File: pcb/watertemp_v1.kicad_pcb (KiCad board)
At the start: 2 copper layers, 56 x 90 mm, 54 parts, among them J1 RN2483 Ext, J2 SWD, J3 I2C, J4 UART1, J5 UART2, Q1 Q_PMOS_GSD, U1 LPC11U24FBD48, U2 RN2483, U3 SHT21, U4 LP5907-Q1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

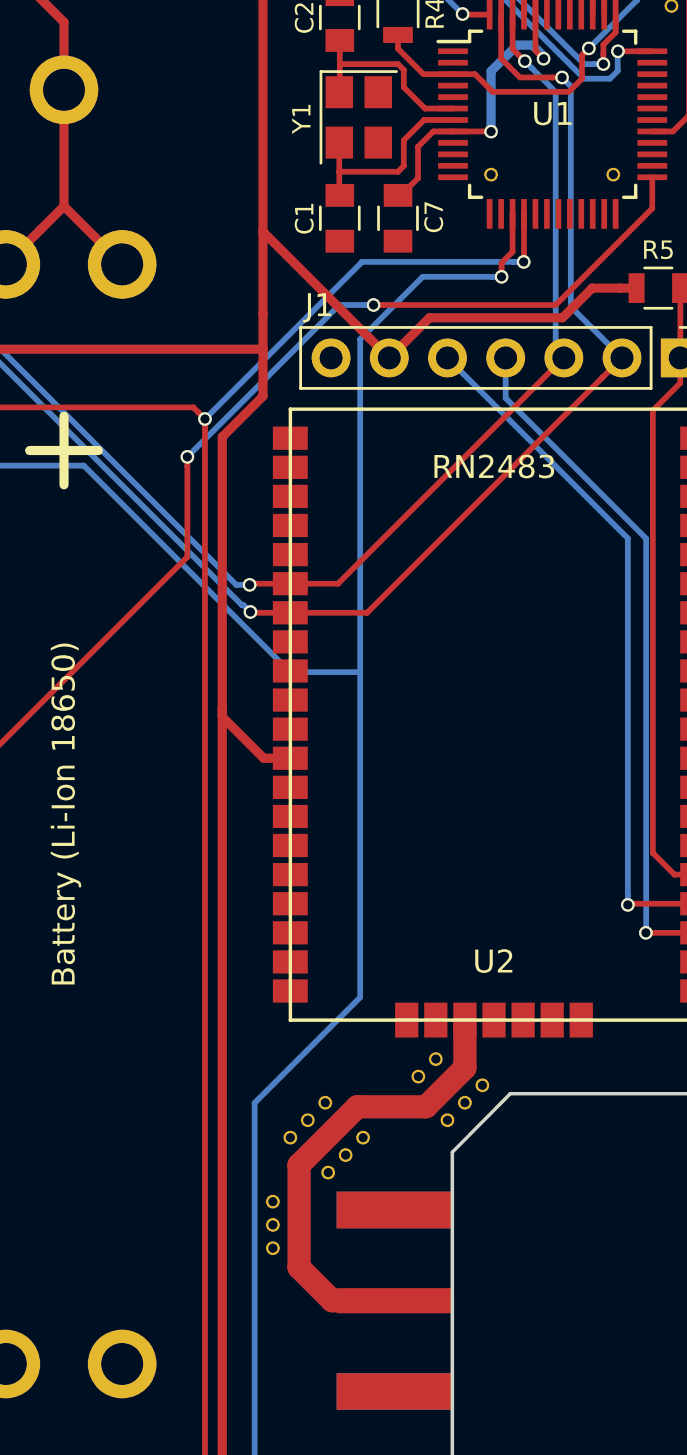
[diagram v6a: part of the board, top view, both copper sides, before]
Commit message: Fix oscillator symbol/footprint (fixes #10)
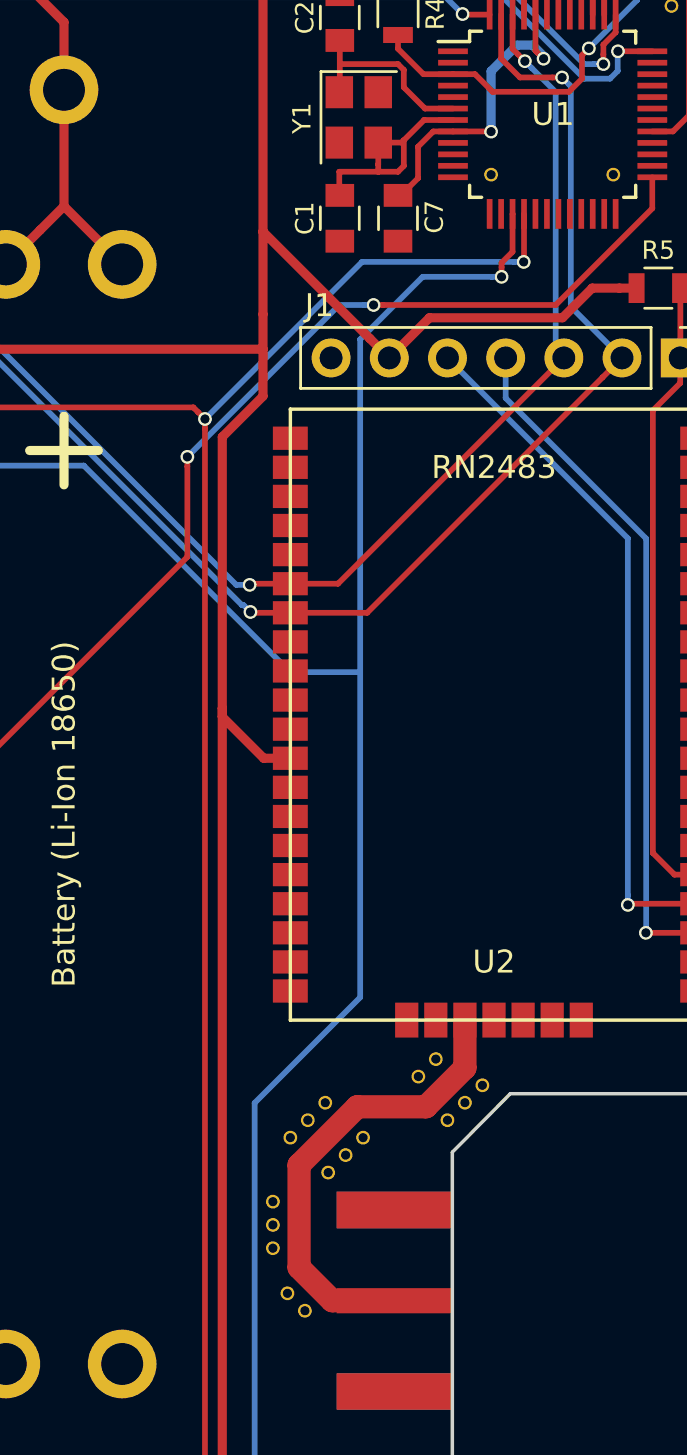
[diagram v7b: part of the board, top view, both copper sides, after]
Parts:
- added REF**: VIA-0.6mm, StitchingVia:VIA-0.6mm, F.Cu at (59.6, 113.5)
- added REF**: VIA-0.6mm, StitchingVia:VIA-0.6mm, F.Cu at (58.8, 112.7)
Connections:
- Y1 pad 2: Net-(C1-Pad1) -> GND
- Y1 pad 3: (no net) -> Net-(C1-Pad1)
- Y1 pad 4: (no net) -> GND
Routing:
- net Net-(C1-Pad1): track 8.87 -> 10.0 mm
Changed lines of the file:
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@@
 (kicad_pcb (version 4) (host pcbnew 4.0.6)
   (general
-    (links 113)
+    (links 120)
     (no_connects 0)
     (area 26.924999 39.924999 83.075001 130.075001)
     (thickness 1.6)
     (drawings 28)
-    (tracks 324)
+    (tracks 329)
     (zones 0)
-    (modules 54)
+    (modules 56)
     (nets 81)
   )
@@
   )
   (module StitchingVia:VIA-0.6mm (layer F.Cu)
+    (at 59.563 113.4745 90)
+    (fp_text reference REF** (at 0 1.27 90) (layer F.SilkS) hide
+      (effects (font (size 1 1) (thickness 0.15)))
+    )
+    (fp_text value VIA-0.6mm (at 0 -1.27 90) (layer F.Fab) hide
+      (effects (font (size 1 1) (thickness 0.15)))
+    )
+    (pad 1 thru_hole circle (at 0 0 90) (size 0.6 0.6) (drill 0.4) (layers *.Cu)
+      (net 1 GND) (zone_connect 2))
+  )
+  (module StitchingVia:VIA-0.6mm (layer F.Cu)
+    (at 58.801 112.7125 90)
+    (fp_text reference REF** (at 0 1.27 90) (layer F.SilkS) hide
+      (effects (font (size 1 1) (thickness 0.15)))
+    )
+    (fp_text value VIA-0.6mm (at 0 -1.27 90) (layer F.Fab) hide
+      (effects (font (size 1 1) (thickness 0.15)))
+    )
+    (pad 1 thru_hole circle (at 0 0 90) (size 0.6 0.6) (drill 0.4) (layers *.Cu)
+      (net 1 GND) (zone_connect 2))
+  )
+  (module StitchingVia:VIA-0.6mm (layer F.Cu)
     (at 58.166 110.744)
     (fp_text reference REF** (at 0 1.27) (layer F.SilkS) hide
@@
       (net 5 "Net-(C2-Pad1)"))
     (pad 2 smd rect (at 1.1 0.85 270) (size 1.4 1.2) (layers F.Cu F.Paste F.Mask)
+      (net 1 GND))
+    (pad 3 smd rect (at 1.1 -0.85 270) (size 1.4 1.2) (layers F.Cu F.Paste F.Mask)
       (net 4 "Net-(C1-Pad1)"))
-    (pad 3 smd rect (at 1.1 -0.85 270) (size 1.4 1.2) (layers F.Cu F.Paste F.Mask))
-    (pad 4 smd rect (at -1.1 -0.85 270) (size 1.4 1.2) (layers F.Cu F.Paste F.Mask))
+    (pad 4 smd rect (at -1.1 -0.85 270) (size 1.4 1.2) (layers F.Cu F.Paste F.Mask)
+      (net 1 GND))
     (model ${KISYS3DMOD}/Crystals.3dshapes/Crystal_SMD_SeikoEpson_TSX3225-4pin_3.2x2.5mm.wrl
       (at (xyz 0 0 0))
@@
   (segment (start 49.0474 60.1786) (end 49.0474 65.2586) (width 0.4) (layer F.Cu) (net 3))
   (segment (start 49.0474 65.2586) (end 51.5874 67.7986) (width 0.4) (layer F.Cu) (net 3))
-  (segment (start 61.065 63.754) (end 63.627 63.754) (width 0.25) (layer F.Cu) (net 4))
+  (segment (start 61.065 63.754) (end 62.7634 63.754) (width 0.25) (layer F.Cu) (net 4))
+  (segment (start 62.7634 63.754) (end 63.627 63.754) (width 0.25) (layer F.Cu) (net 4))
+  (segment (start 62.765 62.482) (end 62.765 63.432) (width 0.25) (layer F.Cu) (net 4))
+  (segment (start 62.765 63.432) (end 62.7634 63.4336) (width 0.25) (layer F.Cu) (net 4))
+  (segment (start 62.7634 63.4336) (end 62.7634 63.754) (width 0.25) (layer F.Cu) (net 4))
+  (segment (start 63.881 63.5) (end 63.881 62.3824) (width 0.25) (layer F.Cu) (net 4))
   (segment (start 63.627 63.754) (end 63.881 63.5) (width 0.25) (layer F.Cu) (net 4))
-  (segment (start 63.881 63.5) (end 63.881 62.3824) (width 0.25) (layer F.Cu) (net 4))
+  (segment (start 61.065 63.754) (end 61.065 64.764) (width 0.25) (layer F.Cu) (net 4))
+  (segment (start 61.065 64.764) (end 61.087 64.786) (width 0.25) (layer F.Cu) (net 4))
+  (segment (start 63.881 62.3824) (end 63.7814 62.482) (width 0.25) (layer F.Cu) (net 4))
+  (segment (start 63.7814 62.482) (end 62.765 62.482) (width 0.25) (layer F.Cu) (net 4))
   (segment (start 63.881 62.3824) (end 64.77 61.4934) (width 0.25) (layer F.Cu) (net 4))
   (segment (start 64.77 61.4934) (end 64.7726 61.496) (width 0.25) (layer F.Cu) (net 4))
   (segment (start 64.7726 61.496) (end 66.028 61.496) (width 0.25) (layer F.Cu) (net 4))
-  (segment (start 61.065 63.754) (end 61.065 64.764) (width 0.25) (layer F.Cu) (net 4))
-  (segment (start 61.065 62.482) (end 61.065 63.754) (width 0.25) (layer F.Cu) (net 4))
-  (segment (start 61.065 64.764) (end 61.087 64.786) (width 0.25) (layer F.Cu) (net 4))
   (segment (start 61.087 59.055) (end 63.627 59.055) (width 0.25) (layer F.Cu) (net 5))
   (segment (start 63.627 59.055) (end 63.881 59.309) (width 0.25) (layer F.Cu) (net 5))

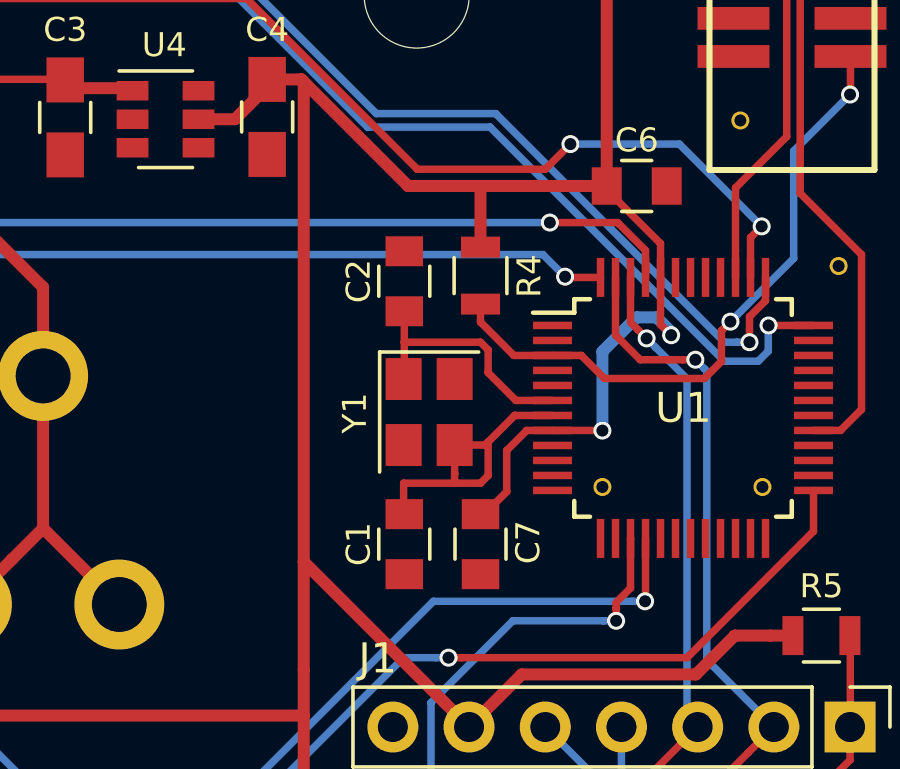
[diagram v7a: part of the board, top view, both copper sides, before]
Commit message: Move oscillator closer µC
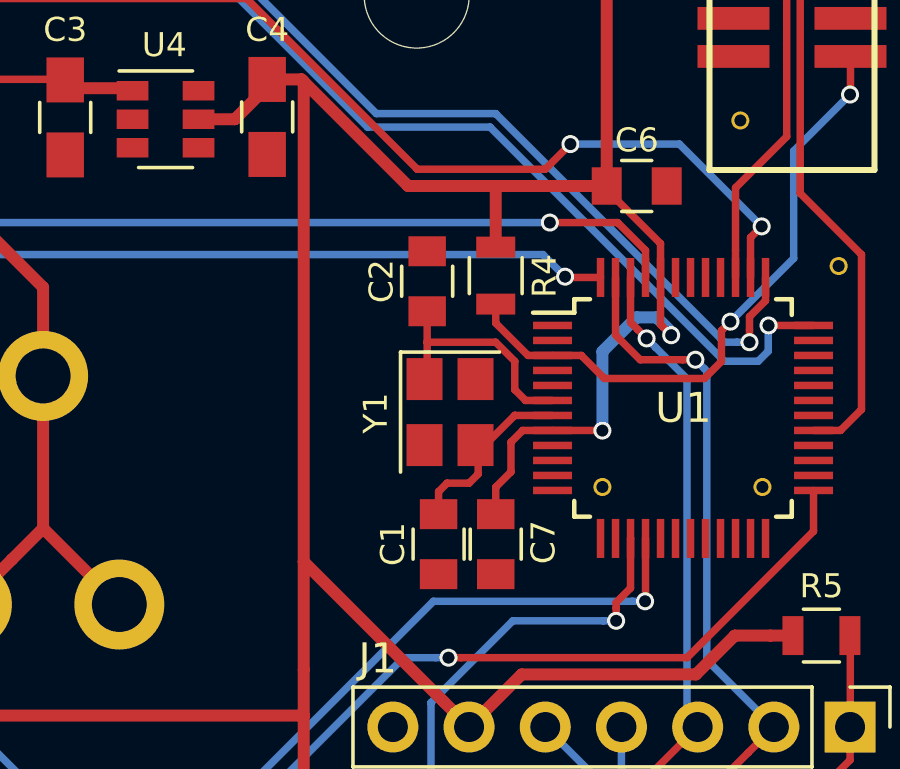
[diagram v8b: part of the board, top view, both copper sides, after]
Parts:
- moved C1 1.14 mm to (62.2, 65.8)
- moved C2 0.76 mm to (61.8, 57.0)
- moved Y1 0.70 mm to (62.6, 61.4)
- moved C7 0.51 mm to (64.1, 65.8)
- moved R4 0.51 mm to (64.1, 56.8)
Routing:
- net Net-(C1-Pad1): track 10.0 -> 5.94 mm
- net Net-(C2-Pad1): track 8.46 -> 7.80 mm
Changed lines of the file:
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@@
-(kicad_pcb (version 4) (host pcbnew 4.0.6)
+(kicad_pcb (version 4) (host pcbnew 4.0.7)
   (general
     (links 120)
-    (no_connects 0)
-    (area 26.924999 39.924999 83.075001 130.075001)
+    (no_connects 4)
+    (area 22.966905 37.719 91.100001 131.826001)
     (thickness 1.6)
     (drawings 28)
-    (tracks 329)
+    (tracks 323)
     (zones 0)
     (modules 56)
@@
   )
   (module Capacitors_SMD:C_0805 (layer F.Cu)
-    (at 61.087 65.786 270)
+    (at 62.23 65.786 270)
     (descr "Capacitor SMD 0805, reflow soldering, AVX (see smccp.pdf)")
     (tags "capacitor 0805")
@@
   )
   (module Capacitors_SMD:C_0805 (layer F.Cu)
-    (at 61.087 57.023 90)
+    (at 61.849 57.023 90)
     (descr "Capacitor SMD 0805, reflow soldering, AVX (see smccp.pdf)")
     (tags "capacitor 0805")
@@
   )
   (module Crystals:Crystal_SMD_Abracon_ABM8G-4pin_3.2x2.5mm (layer F.Cu)
-    (at 61.915 61.382 270)
+    (at 62.611 61.384 270)
     (descr "Abracon Miniature Ceramic Smd Crystal ABM8G http://www.abracon.com/Resonators/ABM8G.pdf, 3.2x2.5mm^2 package")
     (tags "SMD SMT crystal")
@@
   )
   (module Capacitors_SMD:C_0805 (layer F.Cu)
-    (at 63.627 65.786 90)
+    (at 64.135 65.786 90)
     (descr "Capacitor SMD 0805, reflow soldering, AVX (see smccp.pdf)")
     (tags "capacitor 0805")
@@
   )
   (module Resistors_SMD:R_0805 (layer F.Cu)
-    (at 63.627 56.835 270)
+    (at 64.135 56.835 270)
     (descr "Resistor SMD 0805, reflow soldering, Vishay (see dcrcw.pdf)")
     (tags "resistor 0805")
@@
   (segment (start 49.0474 60.1786) (end 49.0474 65.2586) (width 0.4) (layer F.Cu) (net 3))
   (segment (start 49.0474 65.2586) (end 51.5874 67.7986) (width 0.4) (layer F.Cu) (net 3))
-  (segment (start 61.065 63.754) (end 62.7634 63.754) (width 0.25) (layer F.Cu) (net 4))
-  (segment (start 62.7634 63.754) (end 63.627 63.754) (width 0.25) (layer F.Cu) (net 4))
-  (segment (start 62.765 62.482) (end 62.765 63.432) (width 0.25) (layer F.Cu) (net 4))
-  (segment (start 62.765 63.432) (end 62.7634 63.4336) (width 0.25) (layer F.Cu) (net 4))
-  (segment (start 62.7634 63.4336) (end 62.7634 63.754) (width 0.25) (layer F.Cu) (net 4))
-  (segment (start 63.881 63.5) (end 63.881 62.3824) (width 0.25) (layer F.Cu) (net 4))
-  (segment (start 63.627 63.754) (end 63.881 63.5) (width 0.25) (layer F.Cu) (net 4))
-  (segment (start 61.065 63.754) (end 61.065 64.764) (width 0.25) (layer F.Cu) (net 4))
-  (segment (start 61.065 64.764) (end 61.087 64.786) (width 0.25) (layer F.Cu) (net 4))
+  (segment (start 63.246 63.754) (end 63.549 63.451) (width 0.25) (layer F.Cu) (net 4))
+  (segment (start 63.549 63.451) (end 63.549 62.484) (width 0.25) (layer F.Cu) (net 4))
+  (segment (start 62.512 63.754) (end 63.246 63.754) (width 0.25) (layer F.Cu) (net 4))
+  (segment (start 62.23 64.786) (end 62.23 64.036) (width 0.25) (layer F.Cu) (net 4))
+  (segment (start 62.23 64.036) (end 62.512 63.754) (width 0.25) (layer F.Cu) (net 4))
   (segment (start 63.881 62.3824) (end 63.7814 62.482) (width 0.25) (layer F.Cu) (net 4))
-  (segment (start 63.7814 62.482) (end 62.765 62.482) (width 0.25) (layer F.Cu) (net 4))
   (segment (start 63.881 62.3824) (end 64.77 61.4934) (width 0.25) (layer F.Cu) (net 4))
   (segment (start 64.77 61.4934) (end 64.7726 61.496) (width 0.25) (layer F.Cu) (net 4))
   (segment (start 64.7726 61.496) (end 66.028 61.496) (width 0.25) (layer F.Cu) (net 4))
-  (segment (start 61.087 59.055) (end 63.627 59.055) (width 0.25) (layer F.Cu) (net 5))
-  (segment (start 63.627 59.055) (end 63.881 59.309) (width 0.25) (layer F.Cu) (net 5))
-  (segment (start 63.881 59.309) (end 63.881 60.071) (width 0.25) (layer F.Cu) (net 5))
-  (segment (start 63.881 60.071) (end 64.806 60.996) (width 0.25) (layer F.Cu) (net 5))
-  (segment (start 64.806 60.996) (end 66.028 60.996) (width 0.25) (layer F.Cu) (net 5))
-  (segment (start 61.087 59.055) (end 61.087 60.26) (width 0.25) (layer F.Cu) (net 5))
-  (segment (start 61.087 58.023) (end 61.087 59.055) (width 0.25) (layer F.Cu) (net 5))
-  (segment (start 61.087 60.26) (end 61.065 60.282) (width 0.25) (layer F.Cu) (net 5))
+  (segment (start 61.849 59.055) (end 64.13359 59.055) (width 0.25) (layer F.Cu) (net 5))
+  (segment (start 64.13359 59.055) (end 64.77 59.69141) (width 0.25) (layer F.Cu) (net 5))
+  (segment (start 64.77 59.69141) (end 64.77 60.638) (width 0.25) (layer F.Cu) (net 5))
+  (segment (start 65.128 60.996) (end 66.028 60.996) (width 0.25) (layer F.Cu) (net 5))
+  (segment (start 64.77 60.638) (end 65.128 60.996) (width 0.25) (layer F.Cu) (net 5))
+  (segment (start 61.849 59.055) (end 61.849 58.023) (width 0.25) (layer F.Cu) (net 5))
+  (segment (start 61.849 60.284) (end 61.849 59.055) (width 0.25) (layer F.Cu) (net 5))
+  (segment (start 64.135 55.88) (end 64.135 53.848) (width 0.4) (layer F.Cu) (net 6))
+  (segment (start 64.135 64.786) (end 64.135 63.886) (width 0.25) (layer F.Cu) (net 6))
+  (segment (start 64.135 63.886) (end 64.643 63.378) (width 0.25) (layer F.Cu) (net 6))
+  (segment (start 64.643 63.378) (end 64.643 62.385998) (width 0.25) (layer F.Cu) (net 6))
+  (segment (start 64.643 62.385998) (end 65.032998 61.996) (width 0.25) (layer F.Cu) (net 6))
+  (segment (start 65.032998 61.996) (end 66.028 61.996) (width 0.25) (layer F.Cu) (net 6))
   (segment (start 57.7342 66.3702) (end 57.7342 50.368202) (width 0.4) (layer F.Cu) (net 6))
   (segment (start 57.7342 50.368202) (end 57.661998 50.296) (width 0.4) (layer F.Cu) (net 6))
@@
   (segment (start 57.7342 69.977) (end 57.7342 66.3702) (width 0.4) (layer F.Cu) (net 6))
   (segment (start 63.627 53.848) (end 66.548 53.848) (width 0.4) (layer F.Cu) (net 6))
-  (segment (start 63.627 55.885) (end 63.627 55.135) (width 0.4) (layer F.Cu) (net 6))
-  (segment (start 63.627 55.135) (end 63.627 53.848) (width 0.4) (layer F.Cu) (net 6))
   (segment (start 69.628 56.896) (end 69.628 55.767) (width 0.25) (layer F.Cu) (net 6))
   (segment (start 69.628 55.767) (end 67.834 53.973) (width 0.25) (layer F.Cu) (net 6))
@@
   (segment (start 55.9562 87.5474) (end 55.9562 87.1728) (width 0.4) (layer F.Cu) (net 6))
   (segment (start 55.9562 75.331004) (end 57.7342 73.553004) (width 0.4) (layer F.Cu) (net 6))
-  (segment (start 64.502 64.036) (end 63.752 64.786) (width 0.25) (layer F.Cu) (net 6))
   (segment (start 54.229 51.623) (end 55.438 51.623) (width 0.4) (layer F.Cu) (net 6))
   (segment (start 55.438 51.623) (end 56.515 50.546) (width 0.4) (layer F.Cu) (net 6))
-  (segment (start 66.028 61.996) (end 65.167998 61.996) (width 0.25) (layer F.Cu) (net 6))
-  (segment (start 65.167998 61.996) (end 64.502 62.661998) (width 0.25) (layer F.Cu) (net 6))
-  (segment (start 64.502 62.661998) (end 64.502 64.036) (width 0.25) (layer F.Cu) (net 6))
   (segment (start 75.9536 68.834) (end 75.9536 71.8744) (width 0.25) (layer F.Cu) (net 7))
   (segment (start 75.9536 71.8744) (end 75.946 71.882) (width 0.25) (layer F.Cu) (net 7))
@@
   (segment (start 76.327 61.297) (end 75.628 61.996) (width 0.25) (layer F.Cu) (net 13))
   (segment (start 75.628 61.996) (end 74.728 61.996) (width 0.25) (layer F.Cu) (net 13))
+  (segment (start 66.028 59.496) (end 65.211 59.496) (width 0.25) (layer F.Cu) (net 17))
+  (segment (start 64.135 58.42) (end 64.135 57.785) (width 0.25) (layer F.Cu) (net 17))
+  (segment (start 65.211 59.496) (end 64.135 58.42) (width 0.25) (layer F.Cu) (net 17))
   (segment (start 75.946 50.8) (end 74.0664 52.6796) (width 0.25) (layer B.Cu) (net 17))
   (segment (start 74.0664 52.6796) (end 74.0664 56.261) (width 0.25) (layer B.Cu) (net 17))
   (segment (start 74.0664 56.261) (end 71.9582 58.3692) (width 0.25) (layer B.Cu) (net 17))
-  (segment (start 66.028 59.496) (end 64.738 59.496) (width 0.25) (layer F.Cu) (net 17))
-  (segment (start 64.738 59.496) (end 63.627 58.385) (width 0.25) (layer F.Cu) (net 17))
-  (segment (start 63.627 58.385) (end 63.627 57.785) (width 0.25) (layer F.Cu) (net 17))
   (segment (start 67.756201 60.264201) (end 71.089801 60.264201) (width 0.25) (layer F.Cu) (net 17))
   (segment (start 71.089801 60.264201) (end 71.658201 59.695801) (width 0.25) (layer F.Cu) (net 17))
